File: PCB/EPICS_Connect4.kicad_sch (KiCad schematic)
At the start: 26 parts, among them J1 Power, J4 EndA, J5 EndB, J6 LEDA, J7 LEDB, J8 Motor

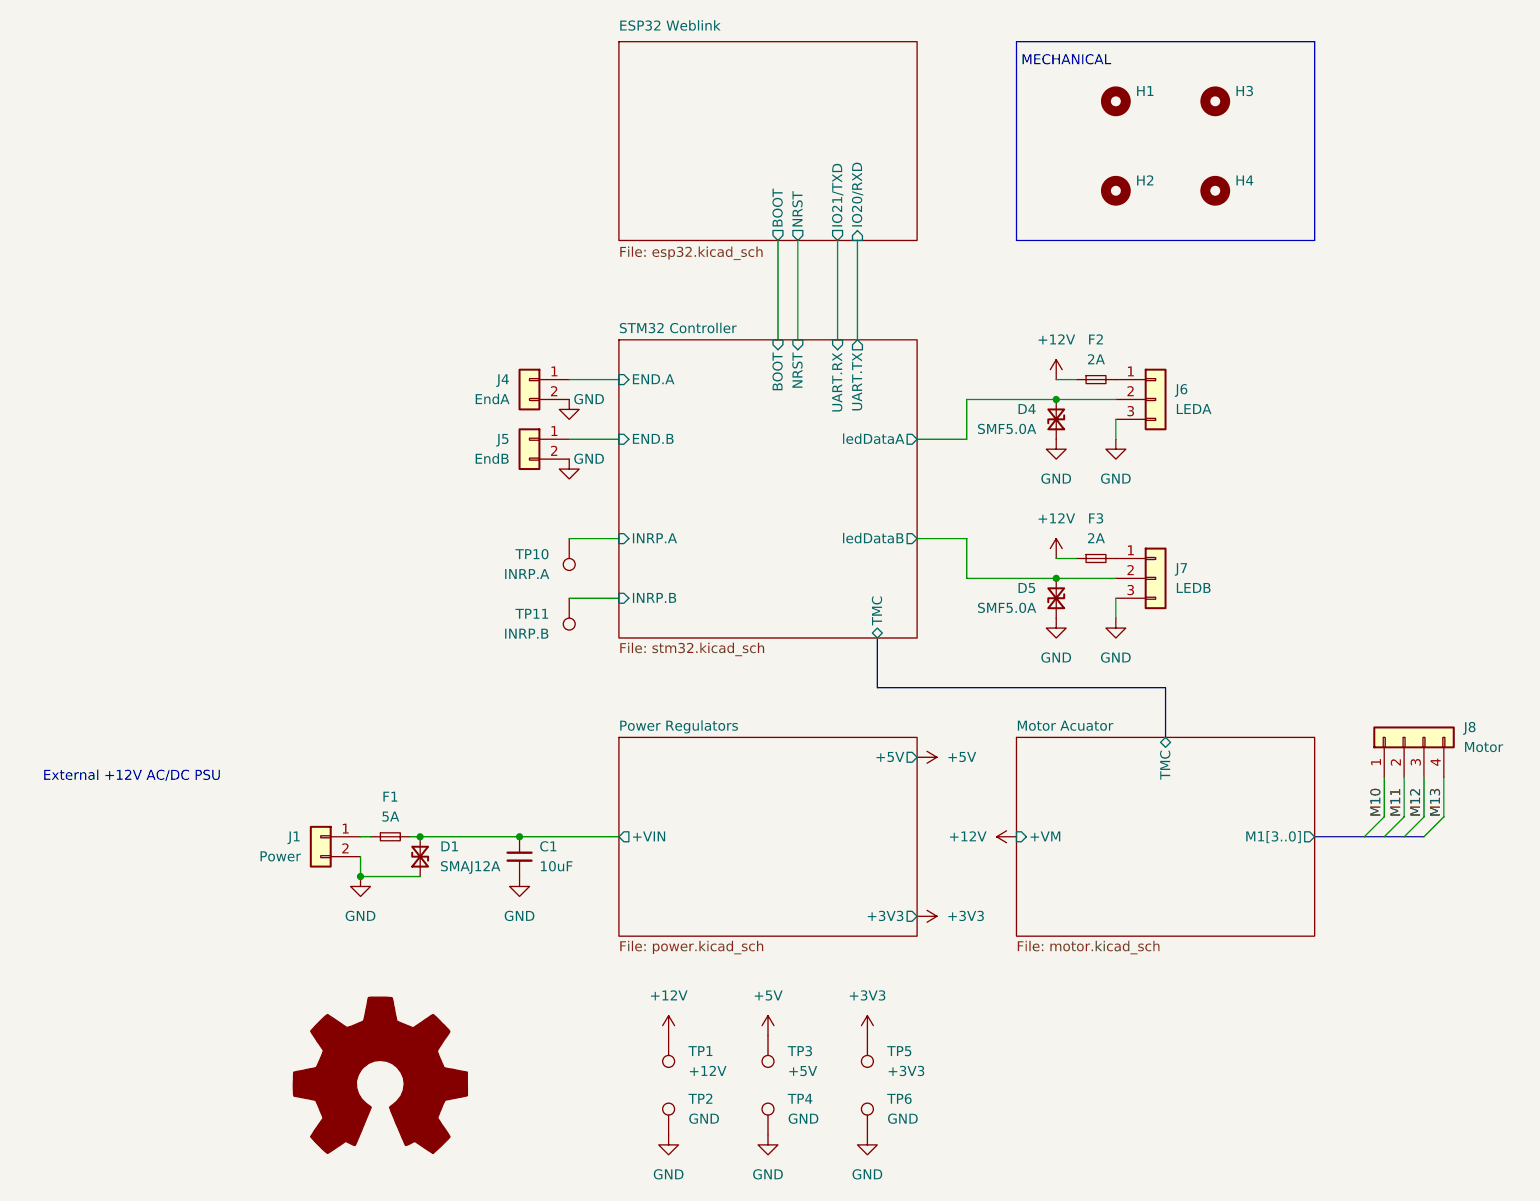
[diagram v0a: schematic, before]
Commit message: Swap Molex connector 3D model to 43650-0215
Co-Authored-By: Claude Opus 5.5 <noreply@anthropic.com>
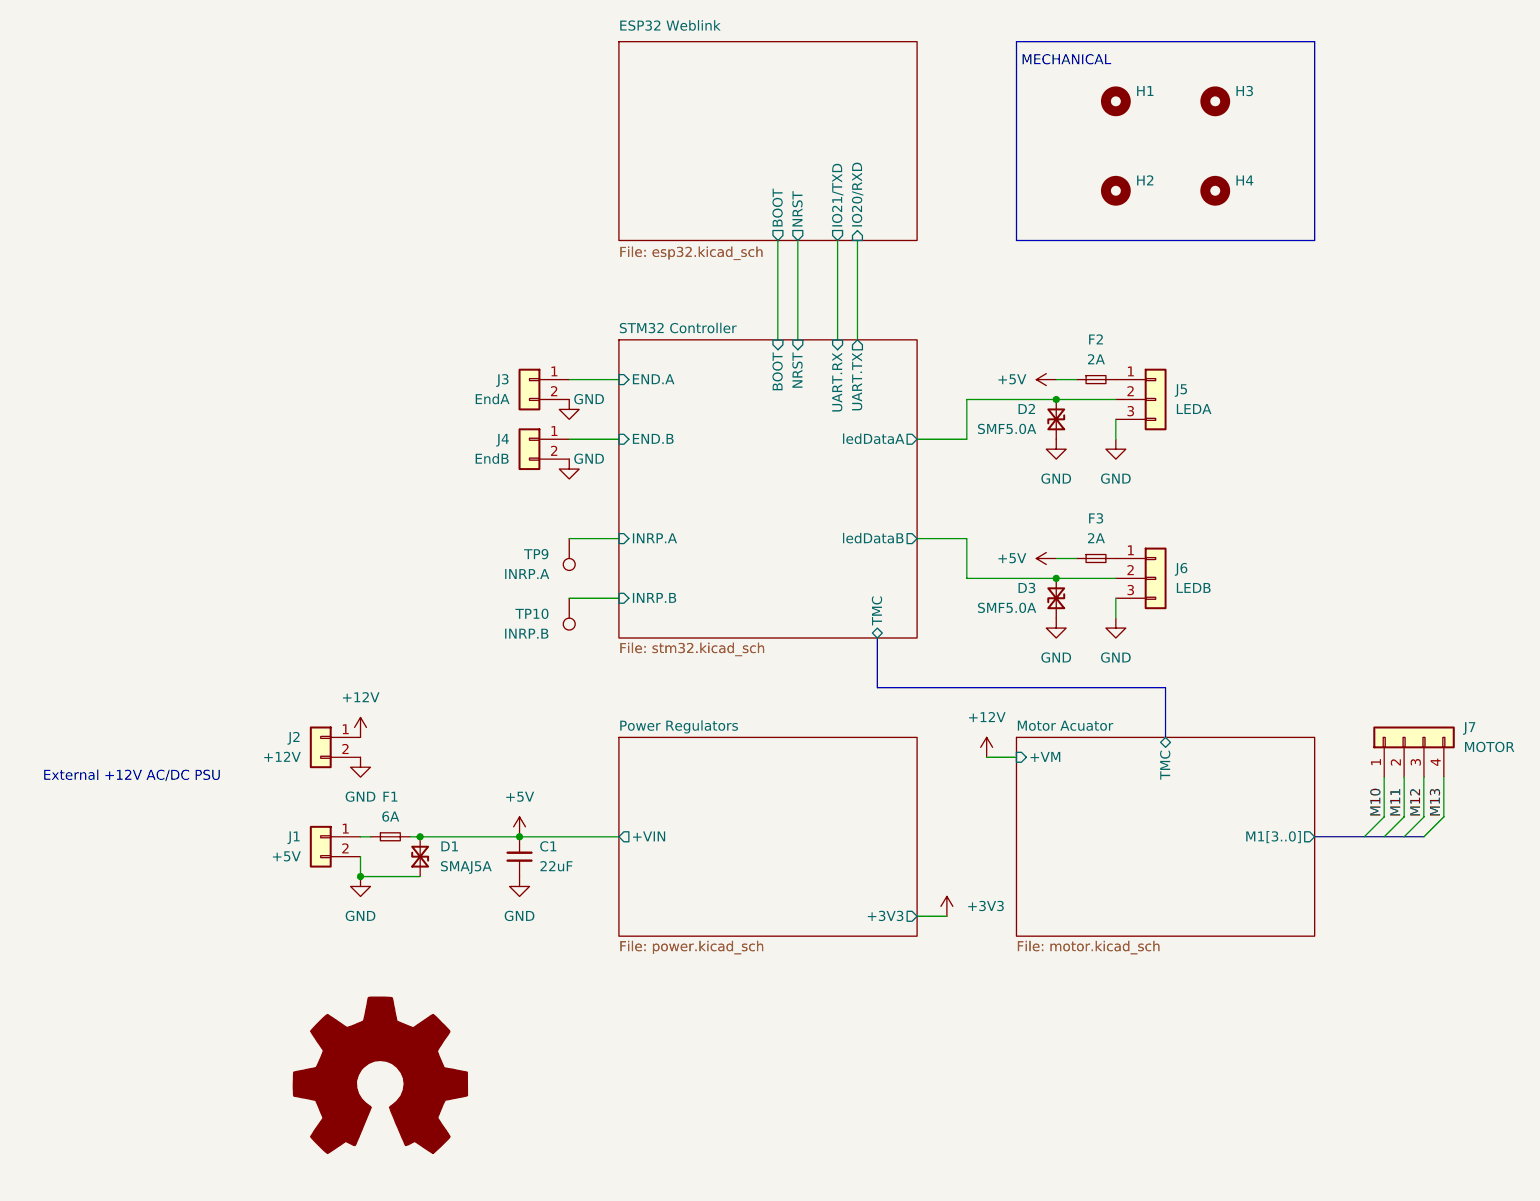
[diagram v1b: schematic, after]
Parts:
- removed TP1: +12V, TestPoint:TestPoint_Pad_1.0x1.0mm, symbol Connector:TestPoint
- removed TP2, TP4, TP6: GND, TestPoint:TestPoint_Pad_1.0x1.0mm, symbol Connector:TestPoint
- removed TP3: +5V, TestPoint:TestPoint_Pad_1.0x1.0mm, symbol Connector:TestPoint
- removed TP5: +3V3, TestPoint:TestPoint_Pad_1.0x1.0mm, symbol Connector:TestPoint
- added J2: +12V, Connector_Molex:Molex_Micro-Fit_3.0_43650-0215_1x02_P3.00mm_Vertical, symbol Connector_Generic:Conn_01x02
- C1: value 10uF -> 22uF
- D1: value SMAJ12A -> SMAJ5A
- F1: value 5A -> 6A
- J1: value Power -> +5V; footprint Connector_Molex:Molex_Micro-Fit_3.0_43650-0200_1x02_P3.00mm_Horizontal -> Connector_Molex:Molex_Micro-Fit_3.0_43650-0215_1x02_P3.00mm_Vertical
- J7: renamed from J8; value Motor -> MOTOR
- TP10: renamed from TP11; now left out of the parts list
- TP9: renamed from TP10; now left out of the parts list
- renumbered D4 to D2, D5 to D3, J4 to J3, J5 to J4, J6 to J5, J7 to J6
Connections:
- net Power Regulators/+VIN is gone; now on net +5V: C1.1, D1.2 (A2), F1.2
- net +12V: now also J2.1 (Pin_1); no longer F2.1, F3.1
- net +5V: now also F2.1, F3.1
- net GND: now also J2.2 (Pin_2)
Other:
- sheet Power Regulators ports: added none; removed +5V
